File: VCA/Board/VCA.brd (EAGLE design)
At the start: 101.3 x 62.2 mm, 66 parts, among them IC1 TL074P, T1 BC237, T2 BC237, T3 BC237, T4 BC237, X1 1503_02, X2 1503_02, X3 1503_02, X4 1503_02

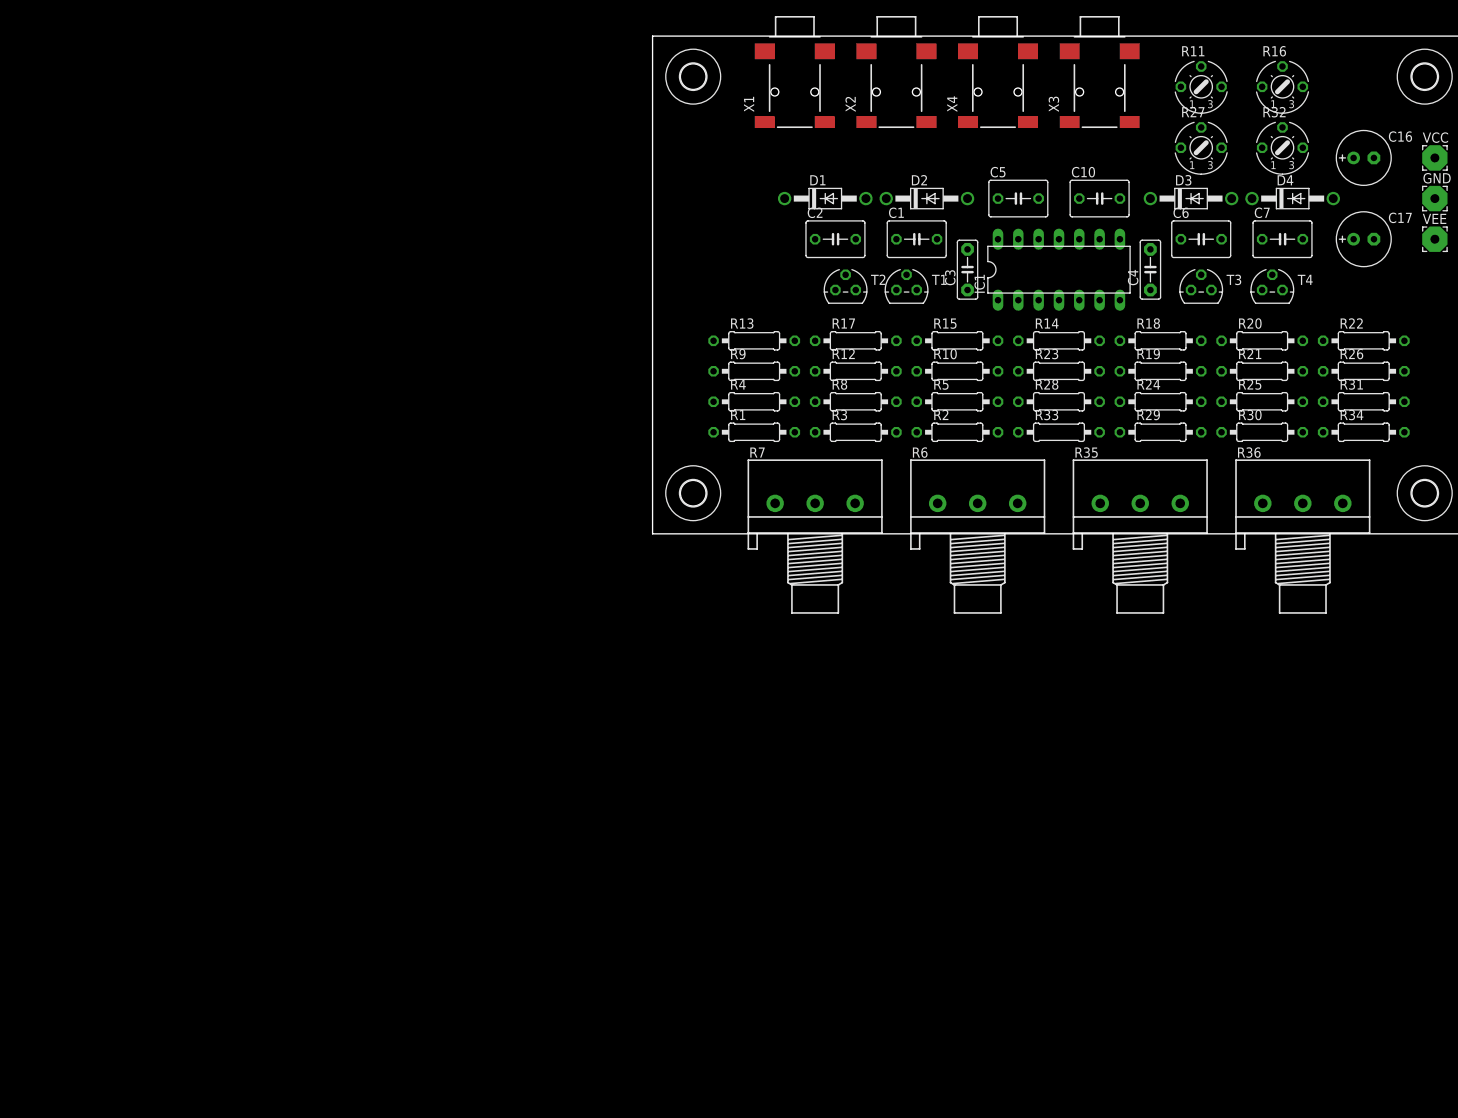
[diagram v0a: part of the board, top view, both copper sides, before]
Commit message: Add VCA schematic
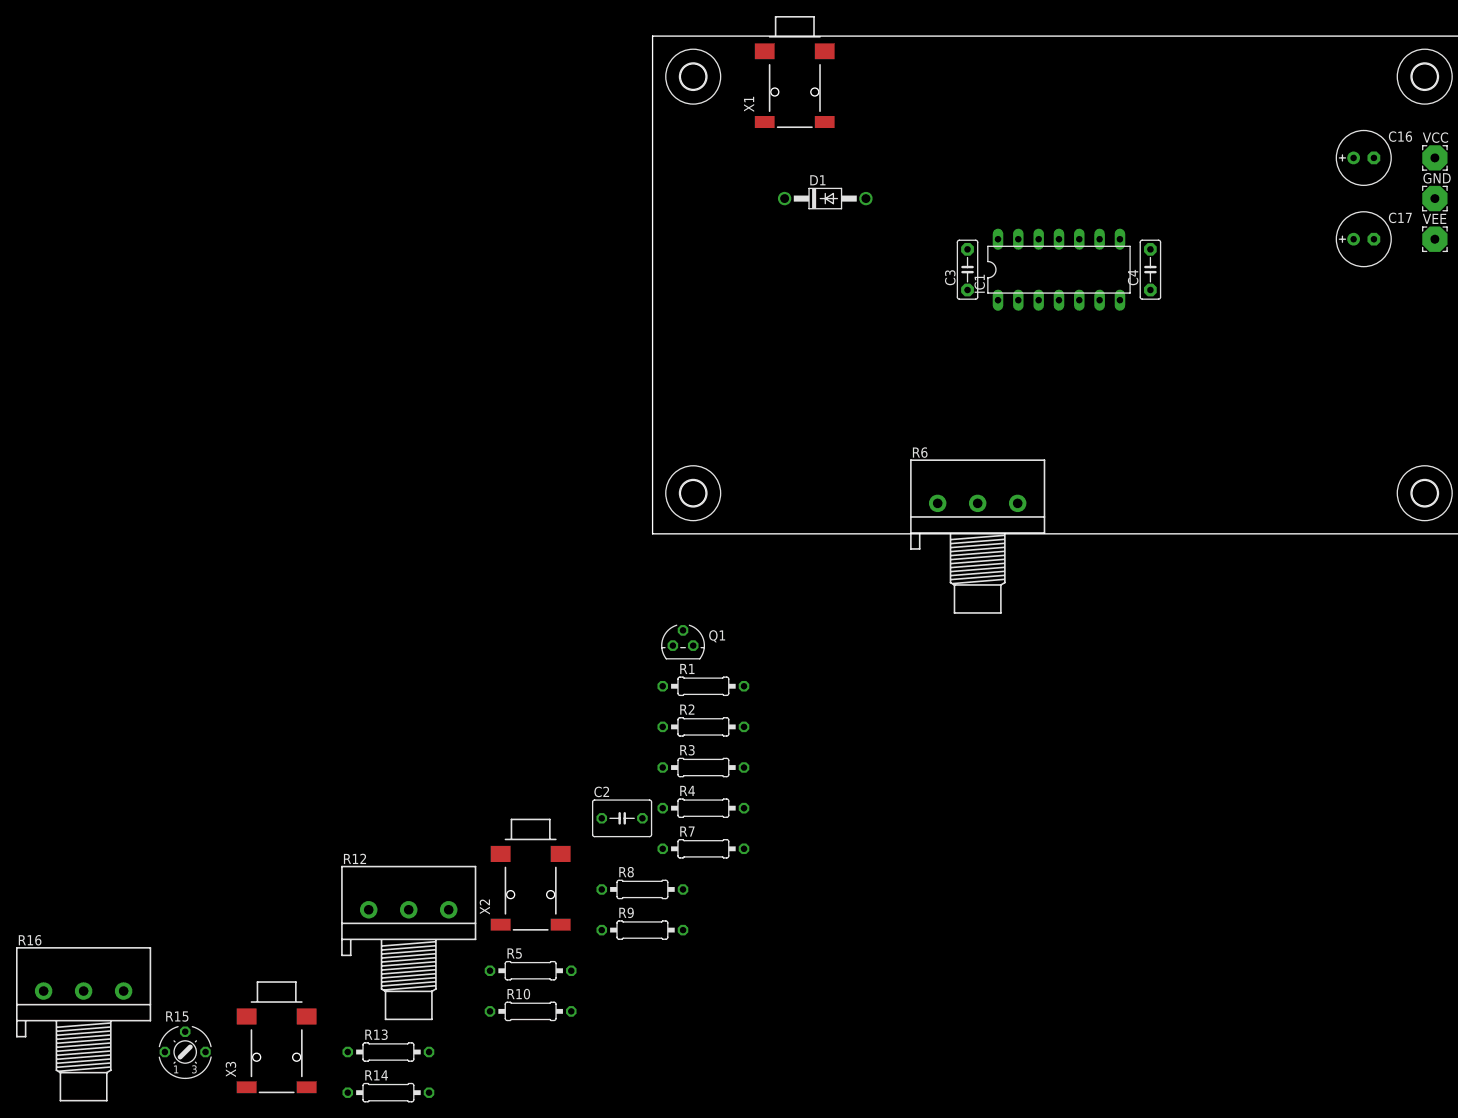
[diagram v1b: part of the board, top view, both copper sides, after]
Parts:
- removed C1, C10, C5, C6, C7: (no value), rcl:C050-045X075
- removed D2, D3, D4: 1N4004, diode:DO41-10
- removed R11, R27, R32: (no value), pot:S75P
- removed R17, R18, R19, R20, R21, R22, R23, R24, R25, R26, R28, R29, R30, R31, R33, R34: (no value), rcl:0207/10
- removed R35, R36: 10k, pot:3RP/1610N
- removed T1, T2, T3, T4: BC237, transistor:TO92
- removed X4: 1503_02, con-lumberg:1503_02
- added Q1: J202, transistor-fet:TO92
- R12: value (none) -> 10k; device rcl:0207/10 -> pot:3RP/1610N
- R15: device rcl:0207/10 -> pot:S75P
- R16: value (none) -> 10k; device pot:S75P -> pot:3RP/1610N
- R7: value 10k -> (none); device pot:3RP/1610N -> rcl:0207/10
- moved R16 187.7 mm to (-74.9, -41.9)
- moved X3 158.6 mm to (-50.8, -43.2)
- moved R15 131.2 mm to (-62.2, -49.5)
- moved R14 125.9 mm to (-36.8, -54.6)
- moved X2 110.3 mm to (-19.1, -22.9)
- moved R13 100.0 mm to (-36.8, -49.5)
- moved R10 96.2 mm to (-19.1, -44.5)
- moved R5 88.9 mm to (-19.1, -39.4)
- moved R12 87.5 mm to (-34.3, -31.8)
- moved C2 77.1 mm to (-7.62, -20.3)
- moved R9 71.2 mm to (-5.08, -34.3)
- moved R8 66.5 mm to (-5.08, -29.2)
- moved R4 51.2 mm to (2.54, -19.1)
- moved R2 48.6 mm to (2.54, -8.89)
- moved R3 46.0 mm to (2.54, -14.0)
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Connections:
- removed net N$18: D3.C, R23.1, T4.3
- removed net N$19: C6.2, D3.A, R19.1
- removed net N$20: R16.A, R18.2
- removed net N$21: R16.E, R17.1
- removed net N$22: C6.1, R22.2, T3.2
- removed net N$23: C7.2, R20.1, T4.2
- removed net N$24: C7.1, D4.A, R21.1
- removed net N$25: D4.C, IC1.9, R24.1, T3.3
- removed net N$26: R22.1, R36.3
- removed net N$27: R20.2, R36.1
- removed net N$28: R35.2, R35.3, R36.2
- removed net N$29: IC1.10, R25.1, R26.2
- removed net N$30: IC1.8, R28.2, R30.1
- removed net N$31: R27.A, R29.2
- removed net N$32: R27.E, R28.1
- removed net N$33: C10.1, IC1.14, R31.1, R33.2
- removed net N$34: C10.2, IC1.13, R30.2, R31.2
- removed net N$35: R32.A, R34.2
- removed net N$36: R32.E, R33.1
- removed net N$37: R27.S, X3.2, X3.3
- removed net N$38: R32.S, X4.2, X4.3
- net GND: now also C3.1, C4.1, IC1.10, Q1.2, R12.1, R4.2, R6.1; no longer R10.1, R13.1, R18.1, R26.1, R29.1, R34.1, T1.1, T2.1, T3.1, T4.1, X4.1
- net N$1: now also IC1.3, Q1.3, R1.1; no longer C2.2, R2.1, T2.2
- net N$10: now also R12.3; no longer R16.S
- net N$11: now also IC1.8, R1.2, R5.1; no longer IC1.3, R10.2, R9.1
- net N$12: now also IC1.9, R10.1, R5.2; no longer R11.A, R13.2
- net N$13: now also R10.2; no longer IC1.1, R14.1
- net N$14: now also IC1.13, R13.1, R14.2; no longer R11.E, R12.1
- net N$15: now also R6.3; no longer R11.S
- net N$16: now also R14.1, R16.3; no longer C5.1, IC1.7, R15.1, R17.2
- net N$17: now also IC1.14, R16.1, R16.2, X3.2, X3.3; no longer C5.2, IC1.6, R14.2, R15.2
- net N$2: now also C2.2, Q1.1, R2.1; no longer C2.1, D2.A, R3.1
- net N$3: now also IC1.2, R3.2, R4.1; no longer D1.C, R5.1, T2.3
- net N$4: now also IC1.1, R13.2, R3.1, R7.1; no longer C1.2, D1.A, R1.1
- net N$5: now also C2.1, R7.2; no longer C1.1, R4.2, T1.2
- net N$6: now also R6.2, R9.2; no longer D2.C, IC1.2, R8.1, T1.3
- net N$7: now also D1.A, IC1.7, R8.1; no longer R4.1, R7.3
- net N$8: now also IC1.6, R8.2, R9.1; no longer R2.2, R7.1
- net N$9: now also D1.C, R2.2; no longer R6.2, R6.3, R7.2
- net VCC: now also C3.2; no longer R1.2, R19.2, R21.2, R23.2, R24.2, R25.2, R3.2, R5.2, R8.2, R9.2
- net VEE: now also C4.2

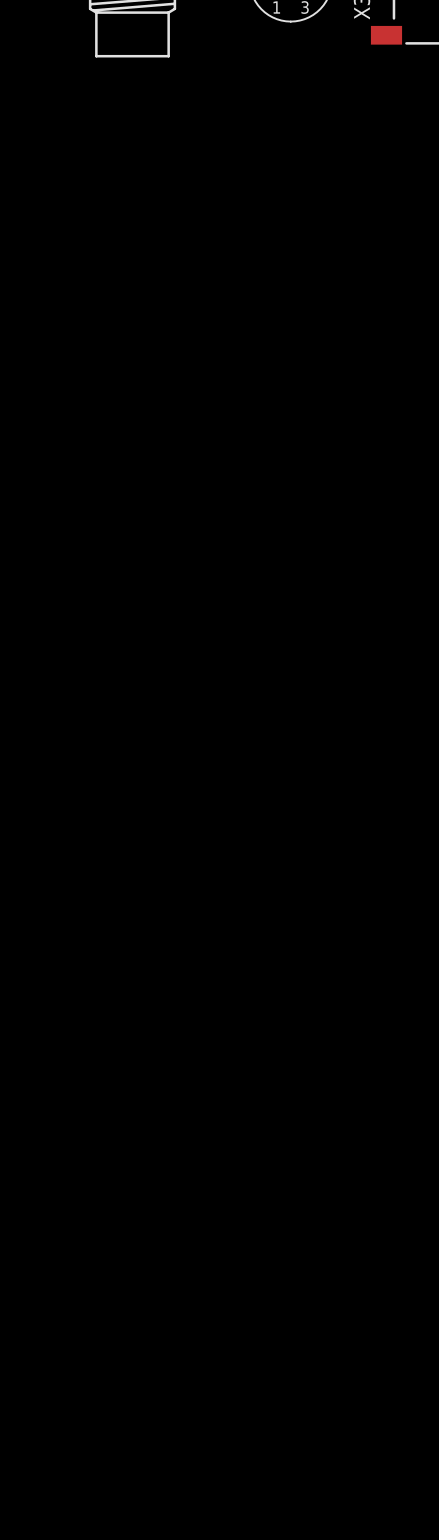
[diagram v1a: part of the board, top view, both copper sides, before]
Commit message: Add clip indicator to VCA
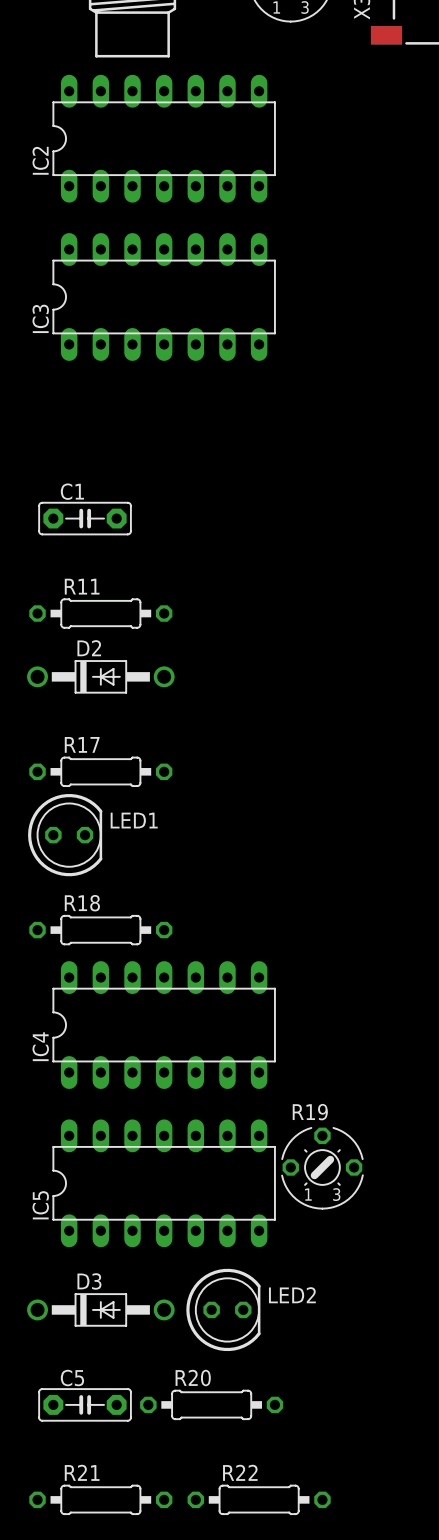
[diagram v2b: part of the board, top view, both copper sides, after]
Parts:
- added C1, C5: 100n, capacitor-wima:C5B2.5
- added D2, D3: 1N4004, diode:DO41-10
- added IC2, IC3, IC4, IC5: TL074P, linear:DIL14
- added LED1, LED2: (no value), led:LED5MM
- added R11, R17, R18, R20, R21, R22: (no value), rcl:0207/10
- added R19: (no value), pot:S75P
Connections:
- new net N$18: D2.A, IC2.1, IC2.2
- new net N$19: C1.2, D2.C, IC3.3, R11.1
- new net N$20: IC3.2, R15.A, R15.S, R17.2
- new net N$22: IC3.1, R18.1
- new net N$23: LED1.A, R18.2
- new net N$25: D3.A, IC4.1, IC4.2
- new net N$26: C5.2, D3.C, IC5.3, R20.1
- new net N$27: IC5.2, R19.A, R19.S, R21.2
- new net N$28: IC5.1, R22.1
- new net N$29: LED2.A, R22.2
- new net V+: IC2.4, IC3.4, IC4.4, IC5.4
- new net V-: IC2.11, IC3.11, IC4.11, IC5.11
- net GND: now also C1.1, C5.1, LED1.K, LED2.K, R11.2, R20.2
- net N$1: now also IC2.3
- net N$2: now also IC4.3
- net VCC: now also R17.1, R21.1

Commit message: VCA board
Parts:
- removed IC2, IC4, IC5: TL074P, linear:DIL14
- added C6, C7: 100n, capacitor-wima:C5B2.5
- moved R20 271.0 mm to (68.6, 69.8)
- moved R19 238.6 mm to (52.1, 66.0)
- moved R21 237.0 mm to (44.5, 31.8)
- moved LED2 230.7 mm to (81.3, 20.3), turned to 90 degrees
- moved R22 227.3 mm to (6.35, 44.5)
- moved R18 224.8 mm to (35.6, 68.6)
- moved C5 222.1 mm to (19.1, 35.6)
- moved D3 209.3 mm to (6.35, 35.6)
- moved LED1 205.9 mm to (72.4, 20.3), turned to 90 degrees
- moved R17 202.1 mm to (25.4, 61.0)
- moved C1 184.1 mm to (53.3, 35.6)
- moved IC3 182.6 mm to (63.5, 47.0)
- moved D2 176.2 mm to (6.35, 49.5)
- moved R13 163.8 mm to (71.1, 73.7)
- moved R14 163.5 mm to (74.9, 64.8)
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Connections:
- net GND: now also C6.1, C7.1
- net N$1: now also IC3.5; no longer IC2.3
- net N$18: now also IC3.6, IC3.7; no longer IC2.1, IC2.2
- net N$2: now also IC3.10; no longer IC4.3
- net N$25: now also IC3.8, IC3.9; no longer IC4.1, IC4.2
- net N$26: now also IC3.12; no longer IC5.3
- net N$27: now also IC3.13; no longer IC5.2
- net N$28: now also IC3.14; no longer IC5.1
- net V+: no longer IC2.4, IC4.4, IC5.4
- net V-: no longer IC2.11, IC4.11, IC5.11
- net VCC: now also C6.2
- net VEE: now also C7.2
